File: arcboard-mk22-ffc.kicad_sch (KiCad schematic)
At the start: 21 parts, among them J10 Conn_01x60, J7 Conn_01x04, J8 Conn_01x04

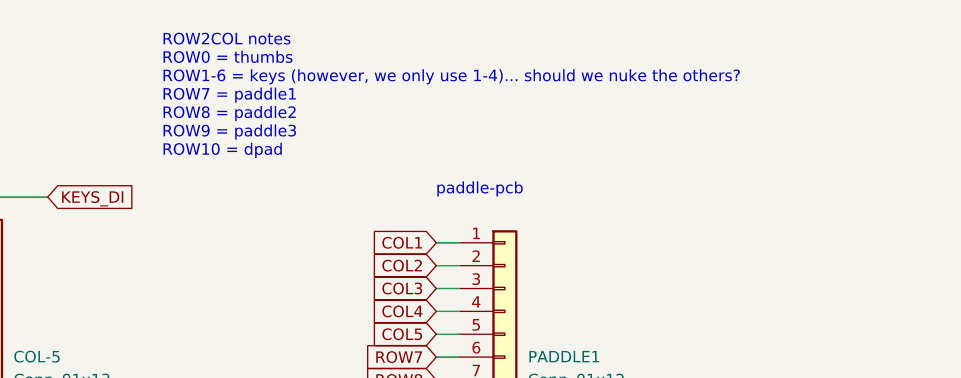
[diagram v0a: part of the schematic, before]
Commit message: fixing folding issues, fattening up the led boards
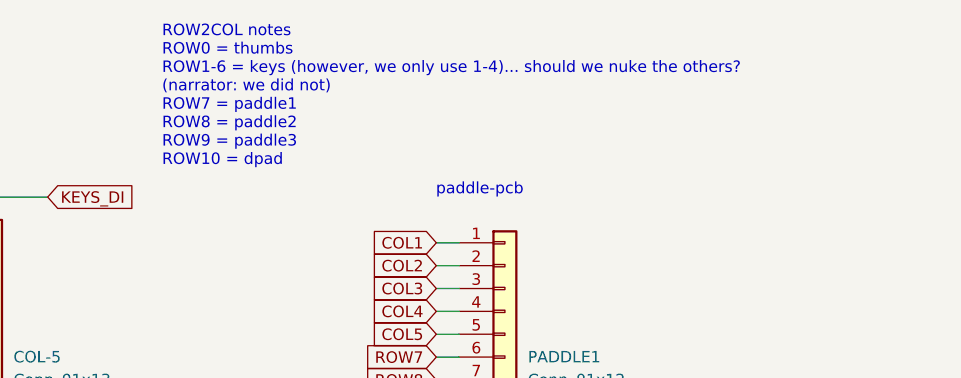
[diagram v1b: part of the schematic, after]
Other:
- note added: "ROW2COL notes ROW0 = thumbs ROW1-6 = keys (however, we only use 1-4)... should we nuke the others? (narrator: we did not) ROW7 = paddle1 ROW8 = paddle2 ROW9 = paddle3 ROW10 = dpad"
- note removed: "ROW2COL notes ROW0 = thumbs ROW1-6 = keys (however, we only use 1-4)... should we nuke the others? ROW7 = paddle1 ROW8 = paddle2 ROW9 = paddle3 ROW10 = dpad"
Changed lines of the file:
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@@
 		)
 	)
-	(text "ROW2COL notes\nROW0 = thumbs\nROW1-6 = keys (however, we only use 1-4)... should we nuke the others?\nROW7 = paddle1\nROW8 = paddle2\nROW9 = paddle3\nROW10 = dpad"
+	(text "ROW2COL notes\nROW0 = thumbs\nROW1-6 = keys (however, we only use 1-4)... should we nuke the others?\n(narrator: we did not)\nROW7 = paddle1\nROW8 = paddle2\nROW9 = paddle3\nROW10 = dpad"
 		(exclude_from_sim no)
 		(at 314.96 30.734 0)

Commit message: first draft silkscreen
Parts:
- added LOGO1, LOGO2: **REF, kicad-libraries:awesome-logo, symbol kicad-libraries:awesome-logo
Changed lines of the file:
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@@
+	)
+	(symbol
+		(lib_id "kicad-libraries:awesome-logo")
+		(at 342.9 147.32 0)
+		(unit 1)
+		(exclude_from_sim no)
+		(in_bom no)
+		(on_board yes)
+		(dnp no)
+		(fields_autoplaced yes)
+		(property "Reference" "LOGO2"
+			(at 345.44 146.0499 0)
+			(effects
+				(font
+					(size 1.27 1.27)
+				)
+				(justify left)
+			)
+		)
+		(property "Value" "**REF"
+			(at 345.44 148.5899 0)
+			(effects
+				(font
+					(size 1.27 1.27)
+				)
+				(justify left)
+			)
+		)
+		(property "Footprint" "kicad-libraries:awesome-logo"
+			(at 342.9 147.32 0)
+			(effects
+				(font
+					(size 1.27 1.27)
+				)
+				(hide yes)
+			)
+		)
+		(property "Datasheet" ""
+			(at 342.9 147.32 0)
+			(effects
+				(font
+					(size 1.27 1.27)
+				)
+				(hide yes)
+			)
+		)
+		(property "Description" "the crazymittens logo"
+			(at 342.9 147.32 0)
+			(effects
+				(font
+					(size 1.27 1.27)
+				)
+				(hide yes)
+			)
+		)
+		(instances
+			(project "arcboard-mk22-ffc"
+				(path "/15943af6-d667-4cb8-b65c-977c058d5764"
+					(reference "LOGO2")
+					(unit 1)
+				)
+			)
+		)
 	)
 	(symbol
@@
 					(unit 1)
 				)
+			)
+		)
+	)
+	(symbol
+		(lib_id "kicad-libraries:awesome-logo")
+		(at 330.2 147.32 0)
+		(unit 1)
+		(exclude_from_sim no)
+		(in_bom no)
+		(on_board yes)
+		(dnp no)
+		(fields_autoplaced yes)
+		(property "Reference" "LOGO1"
+			(at 332.74 146.0499 0)
+			(effects
+				(font
+					(size 1.27 1.27)
+				)
+				(justify left)
+			)
+		)
+		(property "Value" "**REF"
+			(at 332.74 148.5899 0)
+			(effects
+				(font
+					(size 1.27 1.27)
+				)
+				(justify left)
+			)
+		)
+		(property "Footprint" "kicad-libraries:awesome-logo"
+			(at 330.2 147.32 0)
+			(effects
+				(font
+					(size 1.27 1.27)
+				)
+				(hide yes)
+			)
+		)
+		(property "Datasheet" ""
+			(at 330.2 147.32 0)
+			(effects
+				(font
+					(size 1.27 1.27)
+				)
+				(hide yes)
+			)
+		)
+		(property "Description" "the crazymittens logo"
+			(at 330.2 147.32 0)
+			(effects
+				(font
+					(size 1.27 1.27)
+				)
+				(hide yes)
+			)
+		)
+		(instances
+			(project ""
+				(path "/15943af6-d667-4cb8-b65c-977c058d5764"
+					(reference "LOGO1")
+					(unit 1)
+				)

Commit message: first draft readme
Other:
- note added: "Cyboard column PCBs"
- note added: "Cyboard thumb key PCBs"
- note added: "LCD (lcd-adapter-pcb)"
- note added: "dpad (led-pad-pcb)"
- note added: "mainboard (arcboard-stm32-mk2)"
- note added: "paddles (paddle-pcb)"
- note added: "para-led-ogram"
- note added: "ring-encoder (mouse-encoder-pcb)"
- note added: "top-encoder1 (top-encoder-pcb)"
- note added: "top-encoder2 (top-encoder-pcb)"
- note added: "trackball (PMW) (charybdis-pcb)"
- note removed: "is this facing down or up?"
- note removed: "lcd-adapter-pcb"
- note removed: "paddle-pcb"
- note removed: "para-led-ogram (indicators)"
- note removed: "pmw-pcb"
- note removed: "ring-encoder"
- note removed: "top-encoder1"
- note removed: "top-encoder2"
- moved on the sheet: DPAD1, ENC1, ENC3, J10, J7, J8, LOGO1, LOGO2

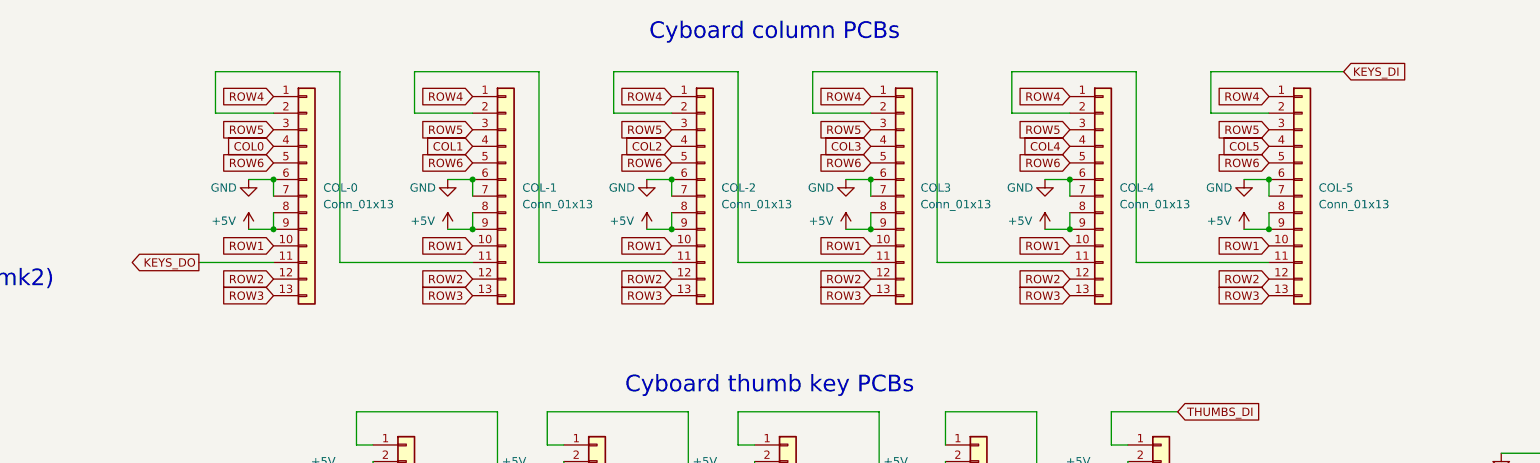
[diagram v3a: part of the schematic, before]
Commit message: fixing 0.3 footprint, the di-do mixup, and starting user comments updates
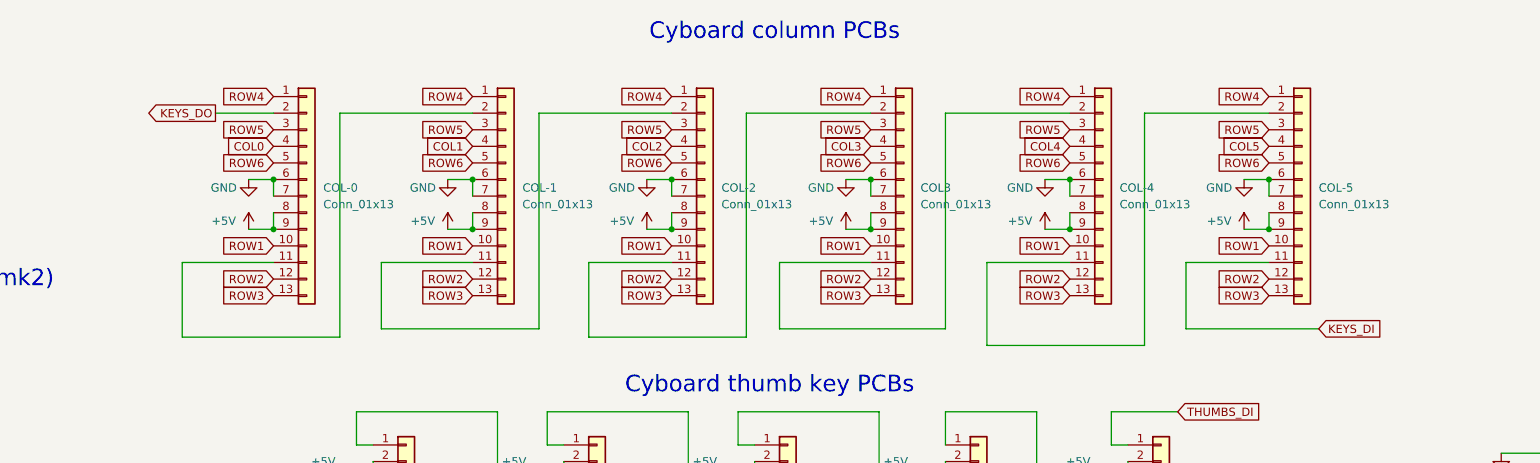
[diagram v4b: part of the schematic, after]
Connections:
- net KEYS_DI: now also COL-5.11 (Pin_11); no longer COL-5.2 (Pin_2)
- net KEYS_DO: now also COL-0.2 (Pin_2); no longer COL-0.11 (Pin_11)
- net at COL-2.11 (Pin_11): now also COL3.2 (Pin_2); no longer COL-1.2 (Pin_2)
- net at COL-2.2 (Pin_2): now also COL-1.11 (Pin_11); no longer COL3.11 (Pin_11)
- net at COL-4.2 (Pin_2): now also COL3.11 (Pin_11); no longer COL-5.11 (Pin_11)
- net at COL-4.11 (Pin_11): now also COL-5.2 (Pin_2); no longer COL3.2 (Pin_2)
- new net: COL-0.11 (Pin_11), COL-1.2 (Pin_2)

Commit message: fixing the reversed pinouts for pmw and lcd-adapter
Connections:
- net +3V3: now also PMW1.1 (Pin_1); no longer PMW1.12 (Pin_12)
- net GND: now also LCD1.2 (Pin_2), LCD1.3 (Pin_3), LCD1.4 (Pin_4), PMW1.2 (Pin_2); no longer LCD1.10 (Pin_10), LCD1.11 (Pin_11), LCD1.9 (Pin_9), PMW1.11 (Pin_11)
- net LCD_3V3: now also LCD1.1 (Pin_1); no longer LCD1.12 (Pin_12)
- net LCD_BL: now also LCD1.5 (Pin_5), LCD1.6 (Pin_6); no longer LCD1.7 (Pin_7), LCD1.8 (Pin_8)
- net LCD_CS: now also LCD1.10 (Pin_10); no longer LCD1.3 (Pin_3)
- net LCD_DC: now also LCD1.9 (Pin_9); no longer LCD1.4 (Pin_4)
- net LCD_RST: now also LCD1.7 (Pin_7); no longer LCD1.6 (Pin_6)
- net PMW_CS: now also PMW1.10 (Pin_10); no longer PMW1.3 (Pin_3)
- net PMW_MOTION: now also PMW1.9 (Pin_9); no longer PMW1.4 (Pin_4)
- net SPI1_CLK: now also LCD1.12 (Pin_12), PMW1.12 (Pin_12); no longer LCD1.1 (Pin_1), PMW1.1 (Pin_1)
- net SPI1_MISO: now also PMW1.11 (Pin_11); no longer PMW1.2 (Pin_2)
- net SPI1_MOSI: now also LCD1.11 (Pin_11), PMW1.8 (Pin_8); no longer LCD1.2 (Pin_2), PMW1.5 (Pin_5)
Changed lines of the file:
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@@
 	(symbol
 		(lib_id "Connector_Generic:Conn_01x12")
-		(at 182.88 231.14 0)
-		(unit 1)
-		(exclude_from_sim no)
-		(in_bom yes)
-		(on_board yes)
-		(dnp no)
-		(fields_autoplaced yes)
+		(at 182.88 233.68 0)
+		(mirror x)
+		(unit 1)
+		(exclude_from_sim no)
+		(in_bom yes)
+		(on_board yes)
+		(dnp no)
 		(property "Reference" "PMW1"
-			(at 185.42 231.1399 0)
+			(at 185.42 233.6801 0)
 			(effects
 				(font
@@
 		)
 		(property "Value" "Conn_01x12"
-			(at 185.42 233.6799 0)
+			(at 185.42 231.1401 0)
 			(effects
 				(font
@@
 		)
 		(property "Footprint" "kicad-libraries:ffc-terminator-12pin_0.5mm"
-			(at 182.88 231.14 0)
+			(at 182.88 233.68 0)
 			(effects
 				(font
@@
 		)
 		(property "Datasheet" "~"
-			(at 182.88 231.14 0)
+			(at 182.88 233.68 0)
 			(effects
 				(font
@@
 		)
 		(property "Description" "Generic connector, single row, 01x12, script generated (kicad-library-utils/schlib/autogen/connector/)"
-			(at 182.88 231.14 0)
+			(at 182.88 233.68 0)
 			(effects
 				(font
@@
 	(symbol
 		(lib_id "Connector_Generic:Conn_01x12")
-		(at 135.89 231.14 0)
-		(unit 1)
-		(exclude_from_sim no)
-		(in_bom yes)
-		(on_board yes)
-		(dnp no)
-		(fields_autoplaced yes)
+		(at 135.89 233.68 0)
+		(mirror x)
+		(unit 1)
+		(exclude_from_sim no)
+		(in_bom yes)
+		(on_board yes)
+		(dnp no)
 		(property "Reference" "LCD1"
-			(at 138.43 231.1399 0)
+			(at 138.43 233.6801 0)
 			(effects
 				(font
@@
 		)
 		(property "Value" "Conn_01x12"
-			(at 138.43 233.6799 0)
+			(at 138.43 231.1401 0)
 			(effects
 				(font
@@
 		)
 		(property "Footprint" "kicad-libraries:ffc-terminator-12pin_0.5mm"
-			(at 135.89 231.14 0)
+			(at 135.89 233.68 0)
 			(effects
 				(font
@@
 		)
 		(property "Datasheet" "~"
-			(at 135.89 231.14 0)
+			(at 135.89 233.68 0)
 			(effects
 				(font
@@
 		)
 		(property "Description" "Generic connector, single row, 01x12, script generated (kicad-library-utils/schlib/autogen/connector/)"
-			(at 135.89 231.14 0)
-			(effects
-				(font
+			(at 135.89 233.68 0)
+			(effects
+				(font

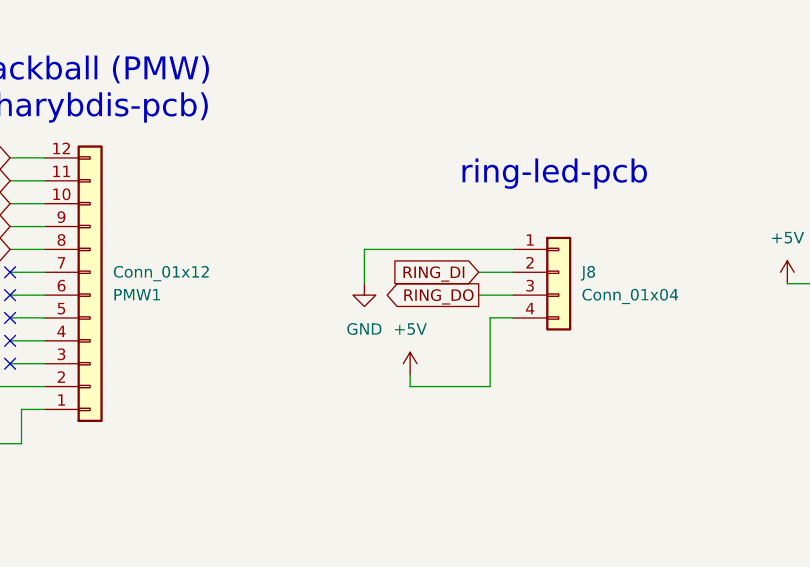
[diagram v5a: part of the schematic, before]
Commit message: updating ring-led-pcb pinouts
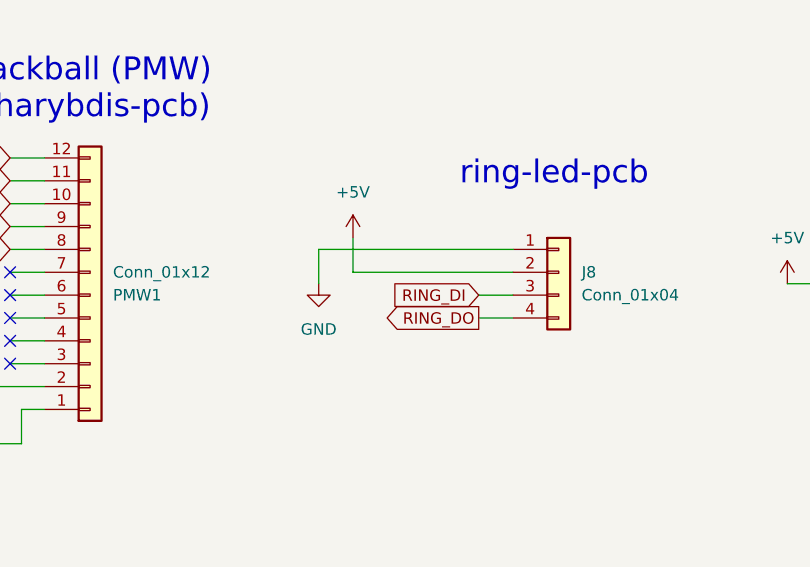
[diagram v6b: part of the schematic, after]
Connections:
- net +5V: now also J8.2 (Pin_2); no longer J8.4 (Pin_4)
- net ENC2_DO: now also J8.3 (Pin_3); no longer J8.2 (Pin_2)
- net Main_LED_OUT: now also J8.4 (Pin_4); no longer J8.3 (Pin_3)
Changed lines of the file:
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@@
 	(wire
 		(pts
+			(xy 226.06 233.68) (xy 229.87 233.68)
+		)
+		(stroke
+			(width 0)
+			(type default)
+		)
+	)
+	(wire
+		(pts
 			(xy 290.83 58.42) (xy 290.83 60.96)
 		)
@@
 	(wire
 		(pts
-			(xy 227.33 236.22) (xy 227.33 243.84)
-		)
-		(stroke
-			(width 0)
-			(type default)
-		)
-	)
-	(wire
-		(pts
 			(xy 190.5 170.18) (xy 209.55 170.18)
 		)
@@
 	(wire
 		(pts
-			(xy 213.36 228.6) (xy 213.36 232.41)
+			(xy 208.28 228.6) (xy 208.28 232.41)
 		)
 		(stroke
@@
 	(wire
 		(pts
-			(xy 226.06 233.68) (xy 229.87 233.68)
-		)
-		(stroke
-			(width 0)
-			(type default)
-		)
-	)
-	(wire
-		(pts
 			(xy 345.44 105.41) (xy 350.52 105.41)
 		)
@@
 	(wire
 		(pts
+			(xy 212.09 231.14) (xy 229.87 231.14)
+		)
+		(stroke
+			(width 0)
+			(type default)
+		)
+	)
+	(wire
+		(pts
 			(xy 261.62 105.41) (xy 269.24 105.41)
 		)
@@
 	(wire
 		(pts
-			(xy 218.44 243.84) (xy 218.44 242.57)
-		)
-		(stroke
-			(width 0)
-			(type default)
-		)
-	)
-	(wire
-		(pts
 			(xy 175.26 105.41) (xy 182.88 105.41)
 		)
@@
 	(wire
 		(pts
-			(xy 229.87 228.6) (xy 213.36 228.6)
+			(xy 229.87 228.6) (xy 208.28 228.6)
 		)
 		(stroke
@@
 	(wire
 		(pts
+			(xy 226.06 236.22) (xy 229.87 236.22)
+		)
+		(stroke
+			(width 0)
+			(type default)
+		)
+	)
+	(wire
+		(pts
 			(xy 247.65 177.8) (xy 252.73 177.8)
 		)
@@
 	(wire
 		(pts
-			(xy 229.87 231.14) (xy 226.06 231.14)
-		)
-		(stroke
-			(width 0)
-			(type default)
-		)
-	)
-	(wire
-		(pts
 			(xy 269.24 119.38) (xy 269.24 121.92)
 		)
@@
 	(wire
 		(pts
-			(xy 227.33 243.84) (xy 218.44 243.84)
+			(xy 265.43 226.06) (xy 283.21 226.06)
 		)
 		(stroke
@@
 	(wire
 		(pts
-			(xy 265.43 226.06) (xy 283.21 226.06)
+			(xy 201.93 124.46) (xy 201.93 93.98)
 		)
 		(stroke
@@
 	(wire
 		(pts
-			(xy 201.93 124.46) (xy 201.93 93.98)
+			(xy 199.39 58.42) (xy 199.39 60.96)
 		)
 		(stroke
@@
 	(wire
 		(pts
-			(xy 199.39 58.42) (xy 199.39 60.96)
+			(xy 212.09 231.14) (xy 212.09 227.33)
 		)
 		(stroke
@@
 	(wire
 		(pts
-			(xy 229.87 236.22) (xy 227.33 236.22)
-		)
-		(stroke
-			(width 0)
-			(type default)
-		)
-	)
-	(wire
-		(pts
 			(xy 72.39 193.04) (xy 81.28 193.04)
 		)
@@
 		)
 	)
+	(global_label "RING_DO"
+		(shape output)
+		(at 226.06 236.22 180)
+		(fields_autoplaced yes)
+		(effects
+			(font
+				(size 1.27 1.27)
+			)
+			(justify right)
+		)
+		(property "Intersheetrefs" "${INTERSHEET_REFS}"
+			(at 215.0314 236.22 0)
+			(effects
+				(font
+					(size 1.27 1.27)
+				)
+				(justify right)
+				(hide yes)
+			)
+		)
+	)
 	(global_label "ROW4"
 		(shape input)
@@
 		)
 	)
-	(global_label "RING_DO"
-		(shape output)
-		(at 226.06 233.68 180)
-		(fields_autoplaced yes)
-		(effects
-			(font
-				(size 1.27 1.27)
-			)
-			(justify right)
-		)
-		(property "Intersheetrefs" "${INTERSHEET_REFS}"
-			(at 215.0314 233.68 0)
-			(effects
-				(font
-					(size 1.27 1.27)
-				)
-				(justify right)
-				(hide yes)
-			)
-		)
-	)
 	(global_label "ROW0"
 		(shape input)
@@
 		)
 	)
+	(global_label "RING_DI"
+		(shape input)
+		(at 226.06 233.68 180)
+		(fields_autoplaced yes)
+		(effects
+			(font
+				(size 1.27 1.27)
+			)
+			(justify right)
+		)
+		(property "Intersheetrefs" "${INTERSHEET_REFS}"
+			(at 215.7571 233.68 0)
+			(effects
+				(font
+					(size 1.27 1.27)
+				)
+				(justify right)
+				(hide yes)
+			)
+		)
+	)
 	(global_label "ROW5"
 		(shape input)
@@
 		)
 	)
-	(global_label "RING_DI"
-		(shape input)
-		(at 226.06 231.14 180)
-		(fields_autoplaced yes)
-		(effects
-			(font
-				(size 1.27 1.27)
-			)
-			(justify right)
-		)
-		(property "Intersheetrefs" "${INTERSHEET_REFS}"
-			(at 215.7571 231.14 0)
-			(effects
-				(font
-					(size 1.27 1.27)
-				)
-				(justify right)
-				(hide yes)
-			)
-		)
-	)
 	(global_label "ENCODER3_R1"
 		(shape output)
@@
 		(lib_name "GND_2")
 		(lib_id "power:GND")
-		(at 213.36 232.41 0)
+		(at 208.28 232.41 0)
 		(unit 1)
 		(exclude_from_sim no)
@@
 		(fields_autoplaced yes)
 		(property "Reference" "#PWR09"
-			(at 213.36 238.76 0)
+			(at 208.28 238.76 0)
 			(effects
 				(font
@@
 		)
 		(property "Value" "GND"
-			(at 213.36 237.49 0)
+			(at 208.28 237.49 0)
 			(effects
 				(font
@@
 		)
 		(property "Footprint" ""
-			(at 213.36 232.41 0)
+			(at 208.28 232.41 0)
 			(effects
 				(font
@@
 		)
 		(property "Datasheet" ""
-			(at 213.36 232.41 0)
+			(at 208.28 232.41 0)
 			(effects
 				(font
@@
 		)
 		(property "Description" "Power symbol creates a global label with name \"GND\" , ground"
-			(at 213.36 232.41 0)
+			(at 208.28 232.41 0)
 			(effects
 				(font
@@
 		(lib_name "+5V_1")
 		(lib_id "power:+5V")
-		(at 218.44 242.57 0)
+		(at 212.09 227.33 0)
 		(unit 1)
 		(exclude_from_sim no)
@@
 		(fields_autoplaced yes)
 		(property "Reference" "#PWR010"
-			(at 218.44 246.38 0)
+			(at 212.09 231.14 0)
 			(effects
 				(font
@@
 		)
 		(property "Value" "+5V"
-			(at 218.44 237.49 0)
+			(at 212.09 222.25 0)
 			(effects
 				(font
@@
 		)
 		(property "Footprint" ""
-			(at 218.44 242.57 0)
+			(at 212.09 227.33 0)
 			(effects
 				(font
@@
 		)
 		(property "Datasheet" ""
-			(at 218.44 242.57 0)
+			(at 212.09 227.33 0)
 			(effects
 				(font
@@
 		)
 		(property "Description" "Power symbol creates a global label with name \"+5V\""
-			(at 218.44 242.57 0)
+			(at 212.09 227.33 0)
 			(effects
 				(font
